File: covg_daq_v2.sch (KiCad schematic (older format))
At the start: 16 parts, among them J1 HDMI_A, J10 HDMI_A, J16 Conn_02x16_Odd_Even, J20 Conn_02x16_Odd_Even, J21 Conn_02x16_Odd_Even, J3 HDMI_A, J5 Conn_02x03_Odd_Even, J6 Conn_02x03_Odd_Even, J7 Conn_02x03_Odd_Even, J8 Conn_02x03_Odd_Even, J9 HDMI_A

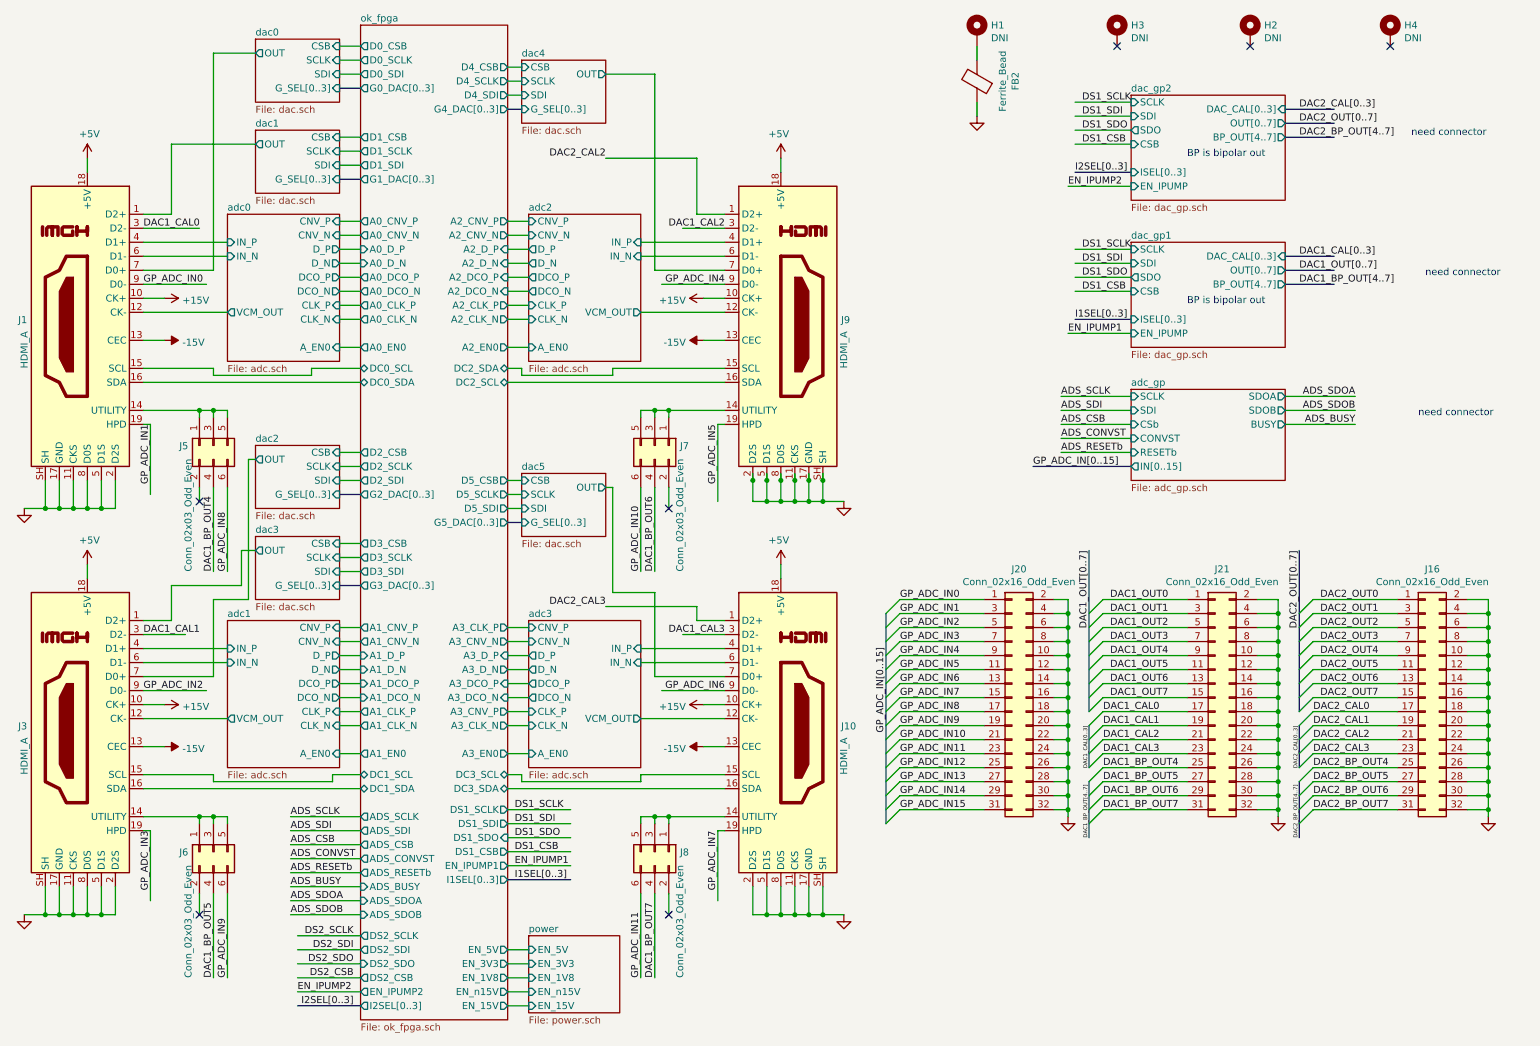
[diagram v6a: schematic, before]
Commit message: added Unique ID chip
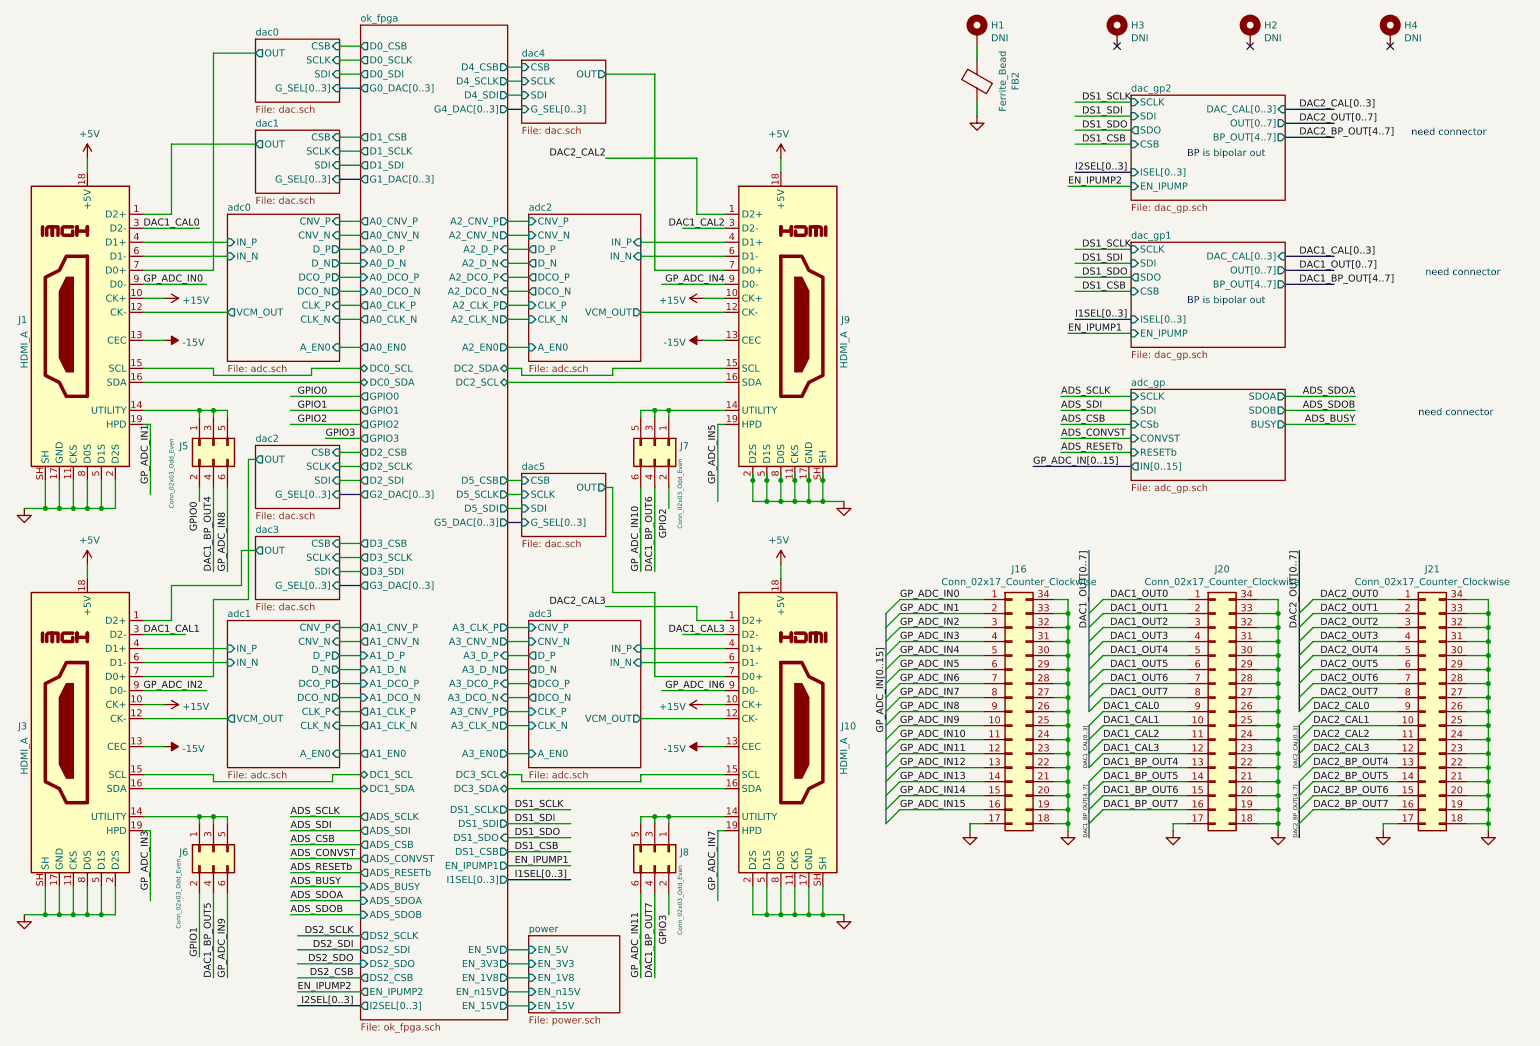
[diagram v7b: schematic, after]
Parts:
- removed J16, J20, J21: Conn_02x16_Odd_Even, symbol Connector_Generic:Conn_02x16_Odd_Even
- added J16, J20, J21: Conn_02x17_Counter_Clockwise, covg-kicad:PinHeader_2x17_P2.00mm_Horizontal, symbol Connector_Generic:Conn_02x17_Counter_Clockwise
- J5, J6, J7, J8: footprint (none) -> Connector_PinHeader_2.00mm:PinHeader_2x03_P2.00mm_Vertical_SMD; Manf# (none) -> 10129383-906002ALF
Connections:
- net labels added: GPIO0, GPIO1, GPIO2, GPIO3
- wire segments 425 -> 441
- no-connect marks 7 -> 3
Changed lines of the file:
@@
 F33 "A0_CLK_N" O L 3000 2700 50
 F34 "A0_D_P" I L 3000 2200 50
-F35 "A0_DCO_N" O L 3000 2500 50
-F36 "A0_DCO_P" O L 3000 2400 50
+F35 "A0_DCO_N" I L 3000 2500 50
+F36 "A0_DCO_P" I L 3000 2400 50
 F37 "ADS_CONVST" O L 3000 6550 50
 F38 "DS1_SDO" I R 4050 6400 50
@@
 F93 "EN_IPUMP1" O R 4050 6600 50
 F94 "EN_IPUMP2" O L 3000 7500 50
+F95 "GPIO0" O L 3000 3250 50
+F96 "GPIO1" O L 3000 3350 50
+F97 "GPIO2" O L 3000 3450 50
+F98 "GPIO3" O L 3000 3550 50
 $EndSheet
 $Sheet
@@
 P 5100 6500
 F 0 "J8" V 5104 6680 50  0000 L CNN
-F 1 "Conn_02x03_Odd_Even" H 5195 6680 50  0000 L CNN
-F 2 "" H 5100 6500 50  0001 C CNN
+F 1 "Conn_02x03_Odd_Even" H 5195 6680 31  0000 L CNN
+F 2 "Connector_PinHeader_2.00mm:PinHeader_2x03_P2.00mm_Vertical_SMD" H 5100 6500 50  0001 C CNN
 F 3 "~" H 5100 6500 50  0001 C CNN
+F 4 "10129383-906002ALF" V 5100 6500 50  0001 C CNN "Manf#"
 	1    5100 6500
-	0    1    1    0
-$EndComp
-$Comp
-L Connector_Generic:Conn_02x03_Odd_Even J6
-U 1 1 613259EF
-P 1950 6500
-F 0 "J6" V 1954 6680 50  0000 L CNN
-F 1 "Conn_02x03_Odd_Even" H 2045 6680 50  0000 L CNN
-F 2 "" H 1950 6500 50  0001 C CNN
-F 3 "~" H 1950 6500 50  0001 C CNN
-	1    1950 6500
-	0    -1   1    0
-$EndComp
-$Comp
-L Connector_Generic:Conn_02x03_Odd_Even J5
-U 1 1 6133DC09
-P 1950 3600
-F 0 "J5" V 1954 3780 50  0000 L CNN
-F 1 "Conn_02x03_Odd_Even" H 2045 3780 50  0000 L CNN
-F 2 "" H 1950 3600 50  0001 C CNN
-F 3 "~" H 1950 3600 50  0001 C CNN
-	1    1950 3600
-	0    -1   1    0
-$EndComp
-$Comp
-L Connector_Generic:Conn_02x03_Odd_Even J7
-U 1 1 61493633
-P 5100 3600
-F 0 "J7" V 5104 3780 50  0000 L CNN
-F 1 "Conn_02x03_Odd_Even" H 5195 3780 50  0000 L CNN
-F 2 "" H 5100 3600 50  0001 C CNN
-F 3 "~" H 5100 3600 50  0001 C CNN
-	1    5100 3600
 	0    1    1    0
 $EndComp
@@
 $EndComp
 $Comp
-L Connector_Generic:Conn_02x16_Odd_Even J20
-U 1 1 615EF5B3
-P 7650 5400
-F 0 "J20" H 7700 6317 50  0000 C CNN
-F 1 "Conn_02x16_Odd_Even" H 7700 6226 50  0000 C CNN
-F 2 "" H 7650 5400 50  0001 C CNN
-F 3 "~" H 7650 5400 50  0001 C CNN
-	1    7650 5400
-	1    0    0    -1
-$EndComp
-$Comp
-L Connector_Generic:Conn_02x16_Odd_Even J21
-U 1 1 61A8FE01
-P 9100 5400
-F 0 "J21" H 9150 6317 50  0000 C CNN
-F 1 "Conn_02x16_Odd_Even" H 9150 6226 50  0000 C CNN
-F 2 "" H 9100 5400 50  0001 C CNN
-F 3 "~" H 9100 5400 50  0001 C CNN
-	1    9100 5400
-	1    0    0    -1
-$EndComp
-$Comp
 L power:GND #PWR0343
 U 1 1 61D8991C
@@
 L power:GND #PWR0340
 U 1 1 60DD2079
-P 9550 6250
-F 0 "#PWR0340" H 9550 6000 50  0001 C CNN
-F 1 "GND" H 9555 6077 50  0001 C CNN
-F 2 "" H 9550 6250 50  0001 C CNN
-F 3 "" H 9550 6250 50  0001 C CNN
-	1    9550 6250
+P 9550 6350
+F 0 "#PWR0340" H 9550 6100 50  0001 C CNN
+F 1 "GND" H 9555 6177 50  0001 C CNN
+F 2 "" H 9550 6350 50  0001 C CNN
+F 3 "" H 9550 6350 50  0001 C CNN
+	1    9550 6350
 	-1   0    0    -1
-$EndComp
-$Comp
-L Connector_Generic:Conn_02x16_Odd_Even J16
-U 1 1 60DD207F
-P 10600 5400
-F 0 "J16" H 10650 6317 50  0000 C CNN
-F 1 "Conn_02x16_Odd_Even" H 10650 6226 50  0000 C CNN
-F 2 "" H 10600 5400 50  0001 C CNN
-F 3 "~" H 10600 5400 50  0001 C CNN
-	1    10600 5400
-	1    0    0    -1
 $EndComp
 $Comp
 L power:GND #PWR0341
 U 1 1 60DD20E0
-P 11050 6250
-F 0 "#PWR0341" H 11050 6000 50  0001 C CNN
-F 1 "GND" H 11055 6077 50  0001 C CNN
-F 2 "" H 11050 6250 50  0001 C CNN
-F 3 "" H 11050 6250 50  0001 C CNN
-	1    11050 6250
+P 11050 6350
+F 0 "#PWR0341" H 11050 6100 50  0001 C CNN
+F 1 "GND" H 11055 6177 50  0001 C CNN
+F 2 "" H 11050 6350 50  0001 C CNN
+F 3 "" H 11050 6350 50  0001 C CNN
+	1    11050 6350
 	-1   0    0    -1
 $EndComp
@@
 L power:GND #PWR0339
 U 1 1 615F19A7
-P 8050 6250
-F 0 "#PWR0339" H 8050 6000 50  0001 C CNN
-F 1 "GND" H 8055 6077 50  0001 C CNN
-F 2 "" H 8050 6250 50  0001 C CNN
-F 3 "" H 8050 6250 50  0001 C CNN
-	1    8050 6250
+P 8050 6350
+F 0 "#PWR0339" H 8050 6100 50  0001 C CNN
+F 1 "GND" H 8055 6177 50  0001 C CNN
+F 2 "" H 8050 6350 50  0001 C CNN
+F 3 "" H 8050 6350 50  0001 C CNN
+	1    8050 6350
 	-1   0    0    -1
 $EndComp
@@
 	1850 6250 1450 6250
 Wire Wire Line
-	1850 6800 1850 6950
-Wire Wire Line
 	2050 6800 2050 7400
 Wire Wire Line
@@
 	7400 850  7400 750
 Wire Wire Line
-	8050 6250 8050 6200
+	8050 6350 8050 6300
 Wire Wire Line
 	8050 6200 7950 6200
@@
 	7450 5800 6850 5800
 Wire Wire Line
-	9550 6250 9550 6200
+	9550 6350 9550 6300
 Wire Wire Line
 	9550 6200 9400 6200
@@
 	6850 6200 7450 6200
 Wire Wire Line
-	11050 6250 11050 6200
+	11050 6350 11050 6300
 Wire Wire Line
 	11050 6200 10900 6200
@@
 Connection ~ 11050 6000
 Connection ~ 11050 6100
-NoConn ~ 1850 4000
-NoConn ~ 1850 6950
-NoConn ~ 5200 6950
-NoConn ~ 5200 4050
 NoConn ~ 8400 750
 NoConn ~ 9350 750
 NoConn ~ 10350 750
+$Comp
+L Connector_Generic:Conn_02x17_Counter_Clockwise J16
+U 1 1 61C544CE
+P 7650 5500
+F 0 "J16" H 7700 6517 50  0000 C CNN
+F 1 "Conn_02x17_Counter_Clockwise" H 7700 6426 50  0000 C CNN
+F 2 "covg-kicad:PinHeader_2x17_P2.00mm_Horizontal" H 7650 5500 50  0001 C CNN
+F 3 "~" H 7650 5500 50  0001 C CNN
+F 4 "Manf#" H 7650 5500 50  0001 C CNN "Field4"
+	1    7650 5500
+	1    0    0    -1
+$EndComp
+$Comp
+L power:GND #PWR0347
+U 1 1 61C58F48
+P 8800 6350
+F 0 "#PWR0347" H 8800 6100 50  0001 C CNN
+F 1 "GND" H 8805 6177 50  0001 C CNN
+F 2 "" H 8800 6350 50  0001 C CNN
+F 3 "" H 8800 6350 50  0001 C CNN
+	1    8800 6350
+	-1   0    0    -1
+$EndComp
+Wire Wire Line
+	8800 6350 8800 6300
+Wire Wire Line
+	8800 6300 8900 6300
+Wire Wire Line
+	7950 6300 8050 6300
+Connection ~ 8050 6300
+Wire Wire Line
+	8050 6300 8050 6200
+$Comp
+L power:GND #PWR0348
+U 1 1 61D18AF5
+P 7350 6350
+F 0 "#PWR0348" H 7350 6100 50  0001 C CNN
+F 1 "GND" H 7355 6177 50  0001 C CNN
+F 2 "" H 7350 6350 50  0001 C CNN
+F 3 "" H 7350 6350 50  0001 C CNN
+	1    7350 6350
+	-1   0    0    -1
+$EndComp
+Wire Wire Line
+	7350 6350 7350 6300
+Wire Wire Line
+	7350 6300 7450 6300
+Wire Wire Line
+	9400 6300 9550 6300
+Connection ~ 9550 6300
+Wire Wire Line
+	9550 6300 9550 6200
+$Comp
+L power:GND #PWR0349
+U 1 1 61DDB491
+P 10300 6350
+F 0 "#PWR0349" H 10300 6100 50  0001 C CNN
+F 1 "GND" H 10305 6177 50  0001 C CNN
+F 2 "" H 10300 6350 50  0001 C CNN
+F 3 "" H 10300 6350 50  0001 C CNN
+	1    10300 6350
+	-1   0    0    -1
+$EndComp
+Wire Wire Line
+	10300 6350 10300 6300
+Wire Wire Line
+	10300 6300 10400 6300
+Wire Wire Line
+	10900 6300 11050 6300
+Connection ~ 11050 6300
+Wire Wire Line
+	11050 6300 11050 6200
+$Comp
+L Connector_Generic:Conn_02x17_Counter_Clockwise J20
+U 1 1 61E7164D
+P 9100 5500
+F 0 "J20" H 9150 6517 50  0000 C CNN
+F 1 "Conn_02x17_Counter_Clockwise" H 9150 6426 50  0000 C CNN
+F 2 "covg-kicad:PinHeader_2x17_P2.00mm_Horizontal" H 9100 5500 50  0001 C CNN
+F 3 "~" H 9100 5500 50  0001 C CNN
+F 4 "Manf#" H 9100 5500 50  0001 C CNN "Field4"
+	1    9100 5500
+	1    0    0    -1
+$EndComp
+$Comp
+L Connector_Generic:Conn_02x17_Counter_Clockwise J21
+U 1 1 61E72858
+P 10600 5500
+F 0 "J21" H 10650 6517 50  0000 C CNN
+F 1 "Conn_02x17_Counter_Clockwise" H 10650 6426 50  0000 C CNN
+F 2 "covg-kicad:PinHeader_2x17_P2.00mm_Horizontal" H 10600 5500 50  0001 C CNN
+F 3 "~" H 10600 5500 50  0001 C CNN
+F 4 "Manf#" H 10600 5500 50  0001 C CNN "Field4"
+	1    10600 5500
+	1    0    0    -1
+$EndComp
+$Comp
+L Connector_Generic:Conn_02x03_Odd_Even J7
+U 1 1 61E7558E
+P 5100 3600
+F 0 "J7" V 5104 3780 50  0000 L CNN
+F 1 "Conn_02x03_Odd_Even" H 5195 3780 31  0000 L CNN
+F 2 "Connector_PinHeader_2.00mm:PinHeader_2x03_P2.00mm_Vertical_SMD" H 5100 3600 50  0001 C CNN
+F 3 "~" H 5100 3600 50  0001 C CNN
+F 4 "10129383-906002ALF" V 5100 3600 50  0001 C CNN "Manf#"
+	1    5100 3600
+	0    1    1    0
+$EndComp
+$Comp
+L Connector_Generic:Conn_02x03_Odd_Even J6
+U 1 1 61E77454
+P 1950 6500
+F 0 "J6" V 1954 6680 50  0000 L CNN
+F 1 "Conn_02x03_Odd_Even" H 2000 6750 31  0000 L CNN
+F 2 "Connector_PinHeader_2.00mm:PinHeader_2x03_P2.00mm_Vertical_SMD" H 1950 6500 50  0001 C CNN
+F 3 "~" H 1950 6500 50  0001 C CNN
+F 4 "10129383-906002ALF" V 1950 6500 50  0001 C CNN "Manf#"
+	1    1950 6500
+	0    -1   1    0
+$EndComp
+$Comp
+L Connector_Generic:Conn_02x03_Odd_Even J5
+U 1 1 61E78915
+P 1950 3600
+F 0 "J5" V 1954 3780 50  0000 L CNN
+F 1 "Conn_02x03_Odd_Even" H 1900 3900 31  0000 L CNN
+F 2 "Connector_PinHeader_2.00mm:PinHeader_2x03_P2.00mm_Vertical_SMD" H 1950 3600 50  0001 C CNN
+F 3 "~" H 1950 3600 50  0001 C CNN
+F 4 "10129383-906002ALF" V 1950 3600 50  0001 C CNN "Manf#"
+	1    1950 3600
+	0    -1   1    0
+$EndComp
+Wire Wire Line
+	3000 3250 2500 3250
+Text Label 2550 3250 0    50   ~ 0
+GPIO0
+Wire Wire Line
+	3000 3350 2500 3350
+Wire Wire Line
+	3000 3450 2500 3450
+Wire Wire Line
+	3000 3550 2750 3550
+Text Label 2550 3350 0    50   ~ 0
+GPIO1
+Text Label 2550 3450 0    50   ~ 0
+GPIO2
+Text Label 2750 3550 0    50   ~ 0
+GPIO3
+Text Label 1850 4000 3    50   ~ 0
+GPIO0
+Text Label 1850 7250 1    50   ~ 0
+GPIO1
+Wire Wire Line
+	1850 6800 1850 7250
+Text Label 5200 4050 3    50   ~ 0
+GPIO2
+Text Label 5200 6950 3    50   ~ 0
+GPIO3
 Wire Bus Line
 	8200 5600 8200 5900

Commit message: layout cleanup; removed custom footrpints
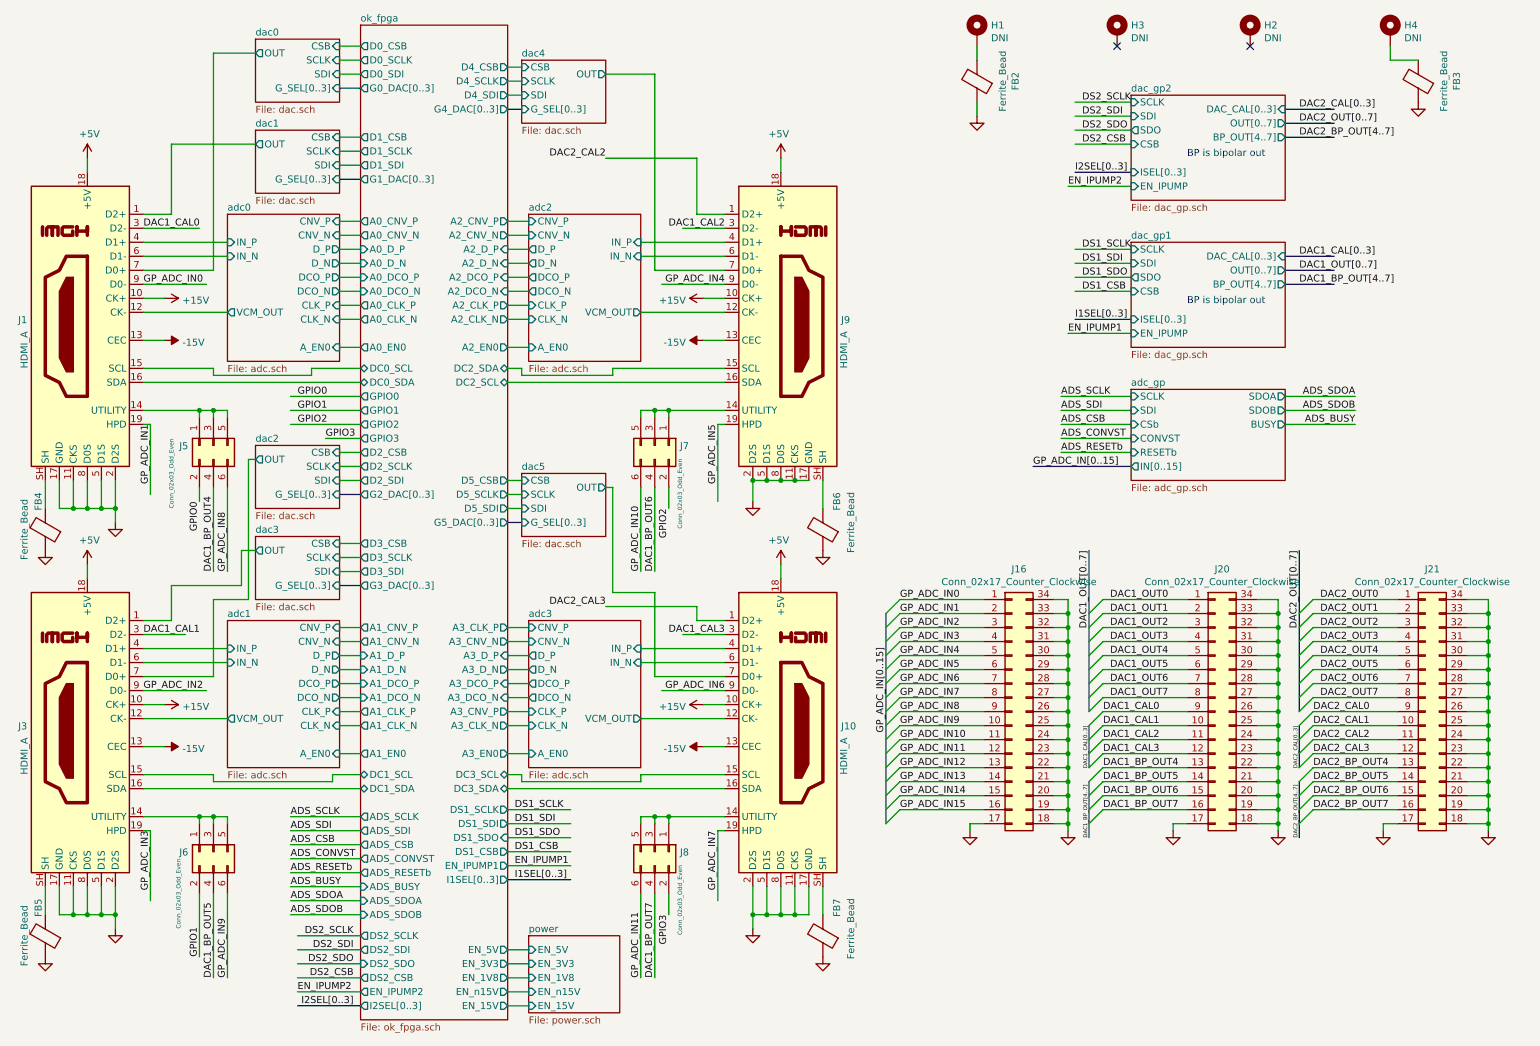
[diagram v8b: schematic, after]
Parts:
- added FB3, FB4, FB5, FB6, FB7: Ferrite_Bead, Capacitor_SMD:C_1206_3216Metric, symbol Device:Ferrite_Bead
- J1, J10, J3, J9: footprint covg-kicad:HDMI_A -> covg-kicad:CONN_10029449-111RLF_HDMI_A
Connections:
- wire segments 441 -> 428
- no-connect marks 3 -> 2
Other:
- note removed: "need connector"
